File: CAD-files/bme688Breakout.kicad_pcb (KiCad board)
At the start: 2 copper layers, 14 x 14.1 mm, 9 parts, among them J1 Conn_01x04_Male, U1 BME688

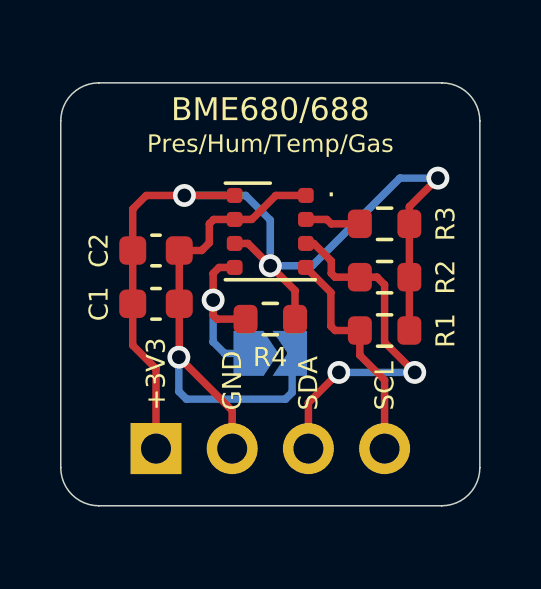
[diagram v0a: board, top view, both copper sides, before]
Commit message: added castellated holes
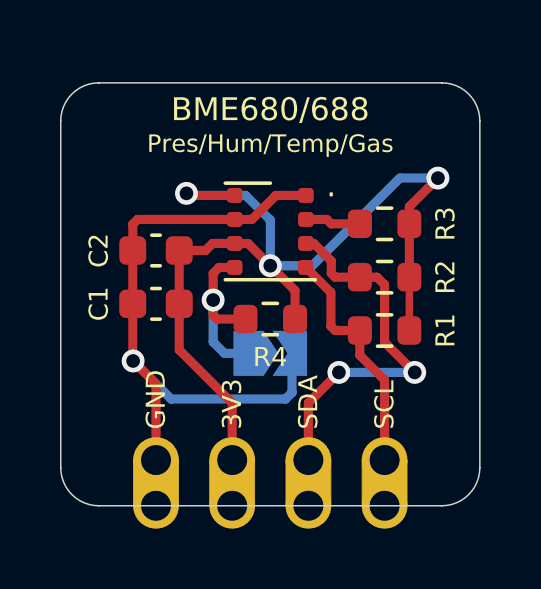
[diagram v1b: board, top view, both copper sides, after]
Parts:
- J1: value Conn_01x04_Male -> Castellated_Conn_01x04; footprint Connector_PinHeader_2.54mm:PinHeader_1x04_P2.54mm_Vertical -> DS-connectors:Castellated_PinHeader_01x04_P2.54mm_Vertical
- moved J1 2.57 mm to (141.0, 108.3)
- turned C1 to 180 degrees
- turned C2 to 180 degrees
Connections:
- J1 pad 1: +3V3 -> GND
- J1 pad 2: GND -> +3V3
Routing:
- net GND: track 19.1 -> 21.6 mm
- net +3V3: track 32.5 -> 31.9 mm
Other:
- board text added: "3V3"
- board text removed: "+3V3"

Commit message: Add files via upload
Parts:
- added J2: Castellated_Conn_01x01, DS-connectors:Castellated_PinHeader_01x01_P2.54mm_Vertical, F.Cu at (141.5, 97.3)
- added J3: Castellated_Conn_01x01, DS-connectors:Castellated_PinHeader_01x01_P2.54mm_Vertical, F.Cu at (149.1, 97.3)
- C1, C2: footprint Capacitor_SMD:C_0603_1608Metric -> Capacitor_SMD:C_0805_2012Metric
- R1, R2, R3, R4: footprint Resistor_SMD:R_0603_1608Metric -> Resistor_SMD:R_0805_2012Metric
- moved C1 0.52 mm to (143.4, 103.6)
- moved R1 0.52 mm to (151.3, 104.5)
- moved R2 0.28 mm to (151.3, 102.5)
- moved R3 0.13 mm to (151.3, 100.5)
- moved C2 0.13 mm to (143.4, 101.3)
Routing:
- net GND: track 21.6 -> 32.8 mm
- net +3V3: track 31.9 -> 32.5 mm
- net SDA: track 12.6 -> 13.2 mm
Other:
- board text added: "BME688"
- board text added: "Temp/Pres/ Hum/Gas"
- board text removed: "BME680/688"
- board text removed: "Pres/Hum/Temp/Gas"
